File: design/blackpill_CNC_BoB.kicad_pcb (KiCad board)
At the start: 4 copper layers, 308 parts, among them J101 ALimIN, J102 ZLimIN, J103 YLimIN, J104 XLimIN, J105 CS_IN, J106 FH_IN, J107 DoorIN, J108 ResetIN, J109 ProbeIN, J110 12V Power in, J111 AuxEncIn, J112 5V Power out, J113 ADC_in_1, J114 ADC_in_2, J115 stepDriverLim, J116 Reset, J117 UART1, J118 I2C, J119 SpindleVFD, J120 Spindle/Coolant, J121 Spindle, J122 Coolant, J123 AuxOut, J124 XStepDrv, J125 YStepDrv, J126 ZStepDrv, J127 AStepDrv, J128 Driver Power in/out, J129 Relais Power in/out, J130 Conn_02x03_Odd_Even, J131 Conn_02x03_Odd_Even, U101 TLP290-4, U102 TLP290-4, U103 TLP290-4, U104 74LVC2G17, U105 LD1117S50TR_SOT223, U106 LM358, U107 TLV9001, U108 TLV9001, U109 YAAJ_WeAct_BlackPill_Part_Like, U110 TLV9001, U111 TLV9001, U112 74HCT541, U113 74HCT541, U114 74HCT541, U115 ULN2003A, U116 ULN2003A, U117 ULN2003A

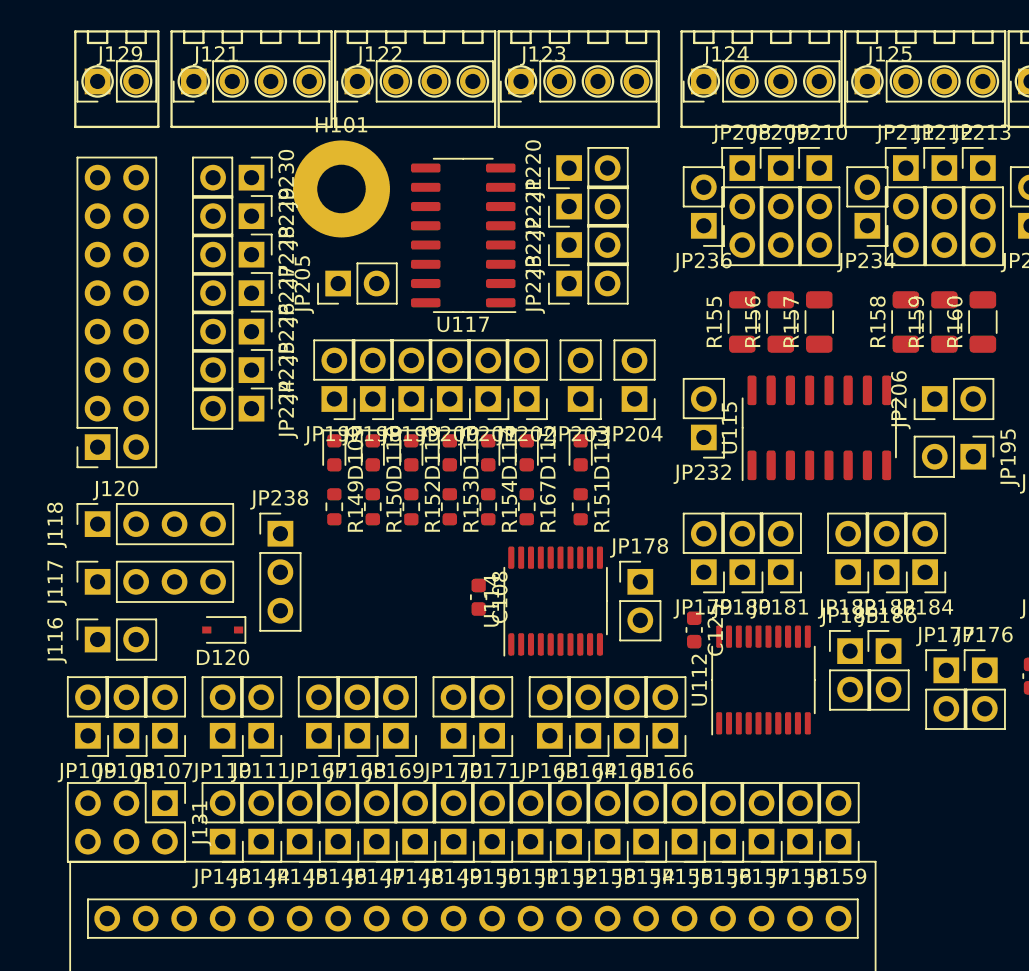
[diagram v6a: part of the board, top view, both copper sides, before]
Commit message: rearrange top left
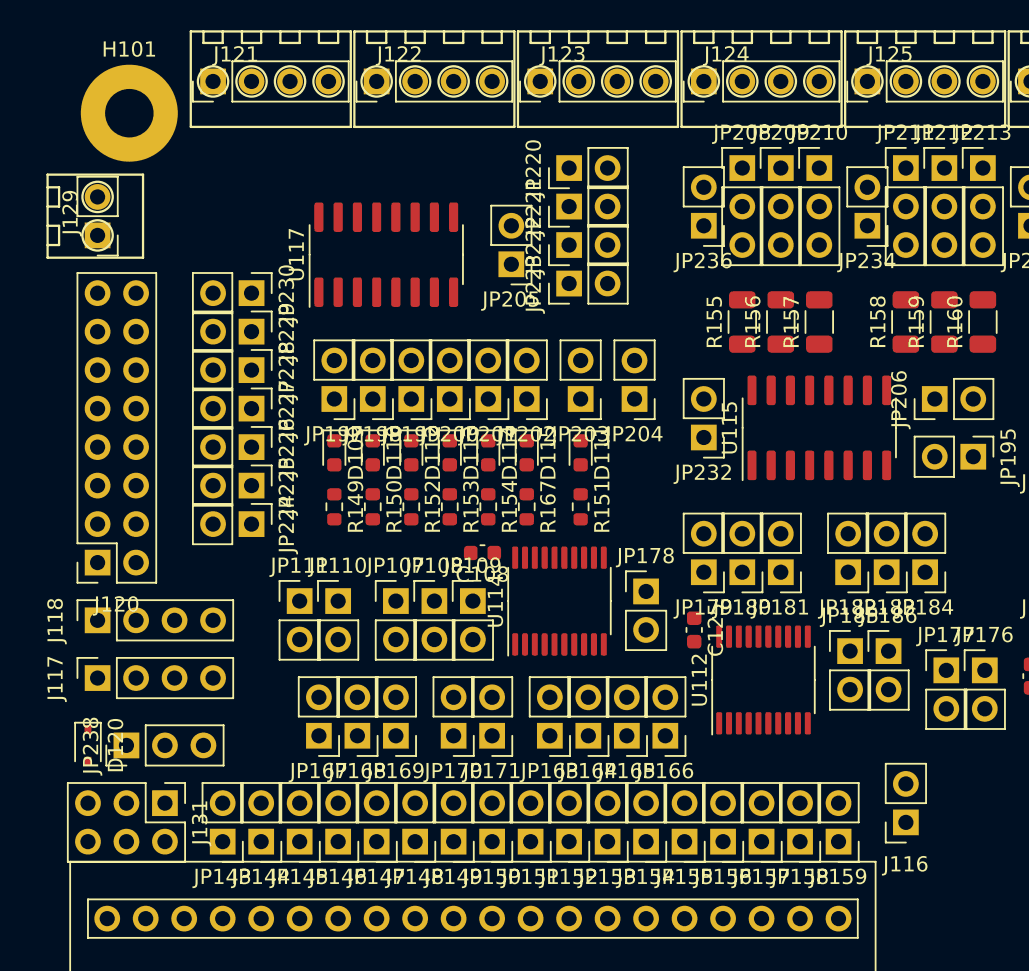
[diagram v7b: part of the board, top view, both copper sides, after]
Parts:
- moved J116 54.7 mm to (55.2, 50.8), turned to 180 degrees
- moved JP109 26.9 mm to (26.7, 36.2), turned to 0 degrees
- moved JP108 22.2 mm to (24.1, 36.2), turned to 0 degrees
- moved JP107 17.6 mm to (21.6, 36.2), turned to 0 degrees
- moved JP238 17.3 mm to (3.81, 45.7), turned to 90 degrees
- moved H101 14.9 mm to (4.00, 4.00)
- moved JP110 11.7 mm to (17.8, 36.2), turned to 0 degrees
- moved D120 11.7 mm to (1.27, 45.7), turned to 270 degrees
- moved JP205 11.5 mm to (29.2, 14.0), turned to 180 degrees
- moved J129 10.2 mm to (1.91, 12.1), turned to 90 degrees
- moved JP111 9.25 mm to (15.2, 36.2), turned to 0 degrees
- moved J120 7.62 mm to (1.91, 33.7)
- moved JP225 7.62 mm to (12.1, 28.6)
- moved JP226 7.62 mm to (12.1, 26.0)
- moved JP227 7.62 mm to (12.1, 23.5)
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
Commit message: rearrange bottom left
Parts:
- moved J116 64.3 mm to (4.45, 90.2), turned to 270 degrees
- moved U104 22.4 mm to (65.4, 73.7)
- moved C101 22.4 mm to (65.4, 76.2)
- moved R111 22.4 mm to (62.2, 73.0)
- moved R113 22.4 mm to (62.2, 76.2)
- moved J105 7.62 mm to (37.5, 98.4)
- moved J109 7.62 mm to (62.9, 98.4)
- moved J103 7.62 mm to (24.8, 98.4)
- moved J101 7.62 mm to (12.1, 98.4)
- moved J102 7.62 mm to (18.4, 98.4)
- moved J104 7.62 mm to (31.1, 98.4)
- moved J106 7.62 mm to (43.8, 98.4)
- moved J107 7.62 mm to (50.2, 98.4)
- moved J108 7.62 mm to (56.5, 98.4)
- moved JP102 5.72 mm to (69.2, 92.1)
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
